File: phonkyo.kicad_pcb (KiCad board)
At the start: 2 copper layers, 65 x 30 mm, 7 parts, among them J1 GPIO, J2 AudioJack3

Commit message: finalize rev2 or v0.2
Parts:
- added C10: 2.2u, Capacitor_SMD:C_0402_1005Metric, F.Cu at (143.0, 85.5)
- added C11: 0.1u, Capacitor_SMD:C_0603_1608Metric, F.Cu at (150.0, 80.7)
- added C12: 0.1u, Capacitor_SMD:C_0402_1005Metric, F.Cu at (153.5, 82.8)
- added C13: 10uf, Capacitor_SMD:C_0603_1608Metric, F.Cu at (155.0, 83.3)
- added C2: 2.2n, Capacitor_SMD:C_0402_1005Metric, F.Cu at (143.0, 90.0)
- added C3: 2.2n, Capacitor_SMD:C_0402_1005Metric, F.Cu at (143.0, 88.0)
- added C4: 2.2u, Capacitor_SMD:C_0402_1005Metric, F.Cu at (146.0, 86.5)
- added C5: 1u, Capacitor_SMD:C_0603_1608Metric, F.Cu at (137.0, 80.0)
- added C6: 2.2n, Capacitor_SMD:C_0402_1005Metric, F.Cu at (151.5, 80.0)
- added C7: 0.1u, Capacitor_SMD:C_0603_1608Metric, F.Cu at (146.0, 81.8)
- added C8: 10uf, Capacitor_SMD:C_0603_1608Metric, F.Cu at (144.0, 81.8)
- added C9: 10uf, Capacitor_SMD:C_0603_1608Metric, F.Cu at (148.5, 80.7)
- added G***: LOGO, LOGO, F.Cu at (113.0, 91.5)
- added J4: RIJack, Connector_Audio:Jack_3.5mm_KoreanHropartsElec_PJ-320D-4A_Horizontal, F.Cu at (120.5, 91.2)
- added JP2: open, Jumper:SolderJumper-2_P1.3mm_Open_RoundedPad1.0x1.5mm, F.Cu at (162.3, 91.0)
- added R10: 22, Resistor_SMD:R_0402_1005Metric, F.Cu at (158.5, 91.0)
- added R11: 0, Resistor_SMD:R_0402_1005Metric, F.Cu at (131.5, 82.0)
- added R3: 470, Resistor_SMD:R_0402_1005Metric, F.Cu at (146.0, 88.5)
- added R4: 470, Resistor_SMD:R_0402_1005Metric, F.Cu at (146.0, 89.5)
- added R5: 10k, Resistor_SMD:R_0402_1005Metric, F.Cu at (153.5, 79.0)
- added R6: 20k, Resistor_SMD:R_0402_1005Metric, F.Cu at (152.5, 80.0)
- added R7: 22, Resistor_SMD:R_0402_1005Metric, F.Cu at (156.5, 77.5)
- added R8: 22, Resistor_SMD:R_0402_1005Metric, F.Cu at (157.5, 77.5)
- added R9: 22, Resistor_SMD:R_0402_1005Metric, F.Cu at (158.5, 90.0)
- added U2: PCM5102A, Package_SO:TSSOP-20_4.4x6.5mm_P0.65mm, F.Cu at (151.1, 88.4)
- added U3: XC6206P332MR, Package_TO_SOT_SMD:SOT-23-3, F.Cu at (140.6, 80.0)
- G***: moved to B.Cu
- J2: value AudioJack3 -> LineOutJack; footprint Connector_Audio:Jack_3.5mm_CUI_SJ-3523-SMT_Horizontal -> Connector_Audio:Jack_3.5mm_KoreanHropartsElec_PJ-320D-4A_Horizontal
- moved J2 5.31 mm to (135.0, 91.2), turned to 90 degrees
- turned G*** to 180 degrees
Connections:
- J2 pad S: GND -> GNDA
- J2 pad T: /GPIO25 -> Net-(C3-Pad2)
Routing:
- net /GPIO18/PCM.CLK: track 0.00 -> 56.5 mm, vias 0 -> 1
- net +5V: track 2.54 -> 50.1 mm, vias 0 -> 1
- net GND: track 14.2 -> 53.5 mm, vias 1 -> 9
- net +3V3: track 21.3 -> 56.8 mm, vias 0 -> 1
- net +3.3VA: track 0.00 -> 19.4 mm, vias 0 -> 2
- net Net-(C3-Pad2): track 0.00 -> 17.0 mm
- net Net-(U2-DIN): track 0.00 -> 16.8 mm
- net Net-(U2-LRCK): track 0.00 -> 16.1 mm
- net Net-(U2-XSMT): track 0.00 -> 15.4 mm
- net Net-(C2-Pad1): track 0.00 -> 15.0 mm
- net /GPIO25: track 14.2 -> 23.7 mm
- net Net-(U2-LDOO): track 0.00 -> 9.28 mm
- net Net-(U2-VNEG): track 0.00 -> 6.12 mm
- net /GPIO19/PCM.FS: track 0.00 -> 5.87 mm
- net /GPIO21/PCM.DOUT: track 0.00 -> 5.35 mm
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- added copper zone on F.Cu, net GNDA
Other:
- board text added: "Audio"
- board text added: "DAC"
- board text added: "Phonkyo v0.2"
- board text added: "Remote"
- board text added: "SCK"
- board text added: "Specs PCM5102A DAC 192kHz 24-bit RI, Line Out 2x 3.5mm Jacks"
- board text removed: "Phonkyo v0.1 Oct. 2024 Be lazier!"

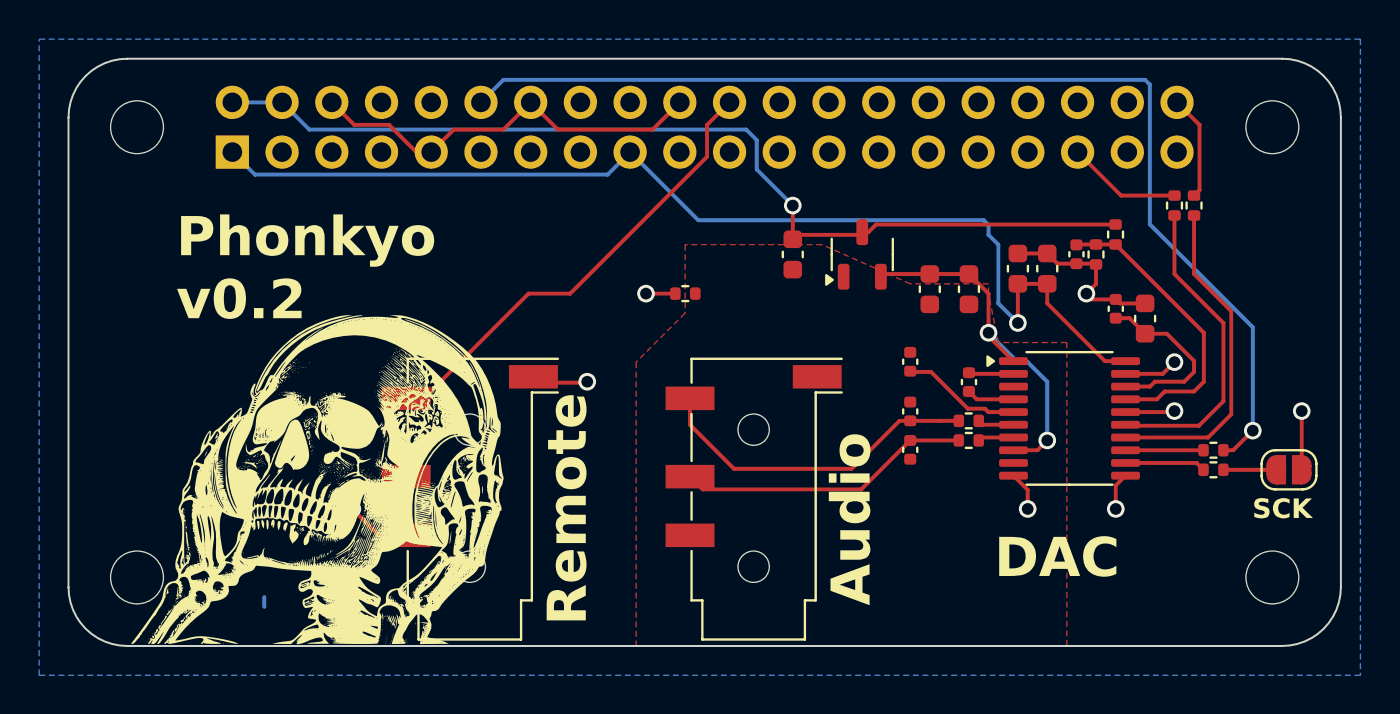
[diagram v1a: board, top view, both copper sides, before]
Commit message: finish BOM for v0.2 and submit to production
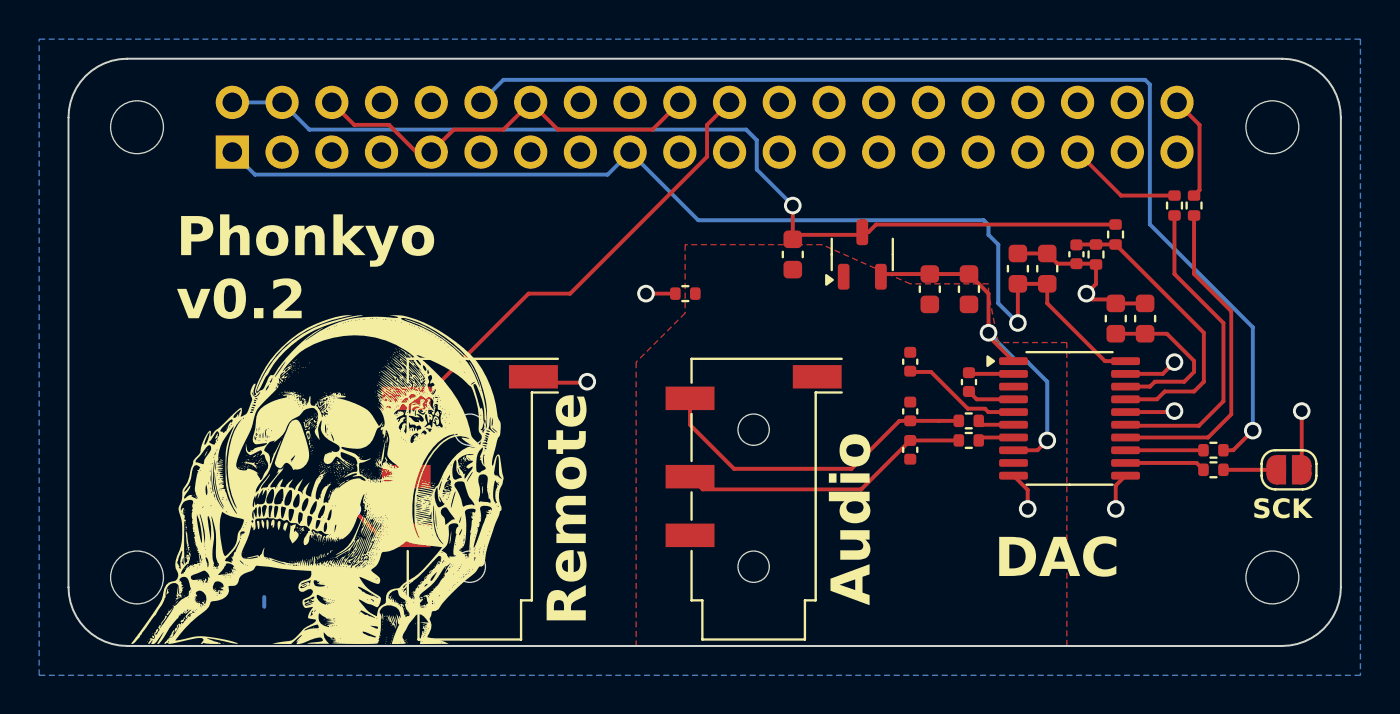
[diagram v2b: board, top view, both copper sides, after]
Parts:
- C12: footprint Capacitor_SMD:C_0402_1005Metric -> Capacitor_SMD:C_0603_1608Metric
- moved C12 0.50 mm to (153.5, 83.3)
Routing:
- net GND: track 53.5 -> 52.4 mm
- net /GPIO25: track 23.7 -> 22.8 mm
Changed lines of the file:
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@@
 			(drillshape 0)
 			(scaleselection 1)
-			(outputdirectory "production/")
+			(outputdirectory "production/v0.2")
 		)
 	)
@@
 		(tags "resistor")
 		(property "Reference" "R3"
-			(at 0 -1.17 360)
+			(at 0 -1.17 0)
 			(layer "F.SilkS")
 			(hide yes)
@@
 		)
 		(property "Value" "470"
-			(at 0 1.17 360)
+			(at 0 1.17 0)
 			(layer "F.Fab")
 			(hide yes)
@@
 		)
 		(fp_text user "${REFERENCE}"
-			(at 0 0 360)
+			(at 0 0 0)
 			(layer "F.Fab")
 			(effects
@@
 		)
 	)
-	(footprint "Capacitor_SMD:C_0402_1005Metric"
+	(footprint "Capacitor_SMD:C_0603_1608Metric"
 		(layer "F.Cu")
-		(at 153.5 82.775 90)
-		(descr "Capacitor SMD 0402 (1005 Metric), square (rectangular) end terminal, IPC_7351 nominal, (Body size source: IPC-SM-782 page 76, https://www.pcb-3d.com/wordpress/wp-content/uploads/ipc-sm-782a_amendment_1_and_2.pdf), generated with kicad-footprint-generator")
+		(at 153.5 83.275 90)
+		(descr "Capacitor SMD 0603 (1608 Metric), square (rectangular) end terminal, IPC_7351 nominal, (Body size source: IPC-SM-782 page 76, https://www.pcb-3d.com/wordpress/wp-content/uploads/ipc-sm-782a_amendment_1_and_2.pdf), generated with kicad-footprint-generator")
 		(tags "capacitor")
 		(property "Reference" "C12"
-			(at 0 -1.16 90)
+			(at 0 -1.43 90)
 			(layer "F.SilkS")
 			(hide yes)
@@
 		)
 		(property "Value" "0.1u"
-			(at 0 1.16 90)
+			(at 0 1.43 90)
 			(layer "F.Fab")
 			(hide yes)
@@
 			)
 		)
-		(property "Footprint" "Capacitor_SMD:C_0402_1005Metric"
+		(property "Footprint" "Capacitor_SMD:C_0603_1608Metric"
 			(at 0 0 90)
 			(unlocked yes)
@@
 		(attr smd)
 		(fp_line
-			(start -0.107836 -0.36)
-			(end 0.107836 -0.36)
+			(start -0.14058 -0.51)
+			(end 0.14058 -0.51)
 			(stroke
 				(width 0.12)
@@
 		)
 		(fp_line
-			(start -0.107836 0.36)
-			(end 0.107836 0.36)
+			(start -0.14058 0.51)
+			(end 0.14058 0.51)
 			(stroke
 				(width 0.12)
@@
 		)
 		(fp_line
-			(start 0.91 -0.46)
-			(end 0.91 0.46)
+			(start 1.48 -0.73)
+			(end 1.48 0.73)
 			(stroke
 				(width 0.05)
@@
 		)
 		(fp_line
-			(start -0.91 -0.46)
-			(end 0.91 -0.46)
+			(start -1.48 -0.73)
+			(end 1.48 -0.73)
 			(stroke
 				(width 0.05)
@@
 		)
 		(fp_line
-			(start 0.91 0.46)
-			(end -0.91 0.46)
+			(start 1.48 0.73)
+			(end -1.48 0.73)
 			(stroke
 				(width 0.05)
@@
 		)
 		(fp_line
-			(start -0.91 0.46)
-			(end -0.91 -0.46)
+			(start -1.48 0.73)
+			(end -1.48 -0.73)
 			(stroke
 				(width 0.05)
@@
 		)
 		(fp_line
-			(start 0.5 -0.25)
-			(end 0.5 0.25)
+			(start 0.8 -0.4)
+			(end 0.8 0.4)
 			(stroke
 				(width 0.1)
@@
 		)
 		(fp_line
-			(start -0.5 -0.25)
-			(end 0.5 -0.25)
+			(start -0.8 -0.4)
+			(end 0.8 -0.4)
 			(stroke
 				(width 0.1)
@@
 		)
 		(fp_line
-			(start 0.5 0.25)
-			(end -0.5 0.25)
+			(start 0.8 0.4)
+			(end -0.8 0.4)
 			(stroke
 				(width 0.1)
@@
 		)
 		(fp_line
-			(start -0.5 0.25)
-			(end -0.5 -0.25)
+			(start -0.8 0.4)
+			(end -0.8 -0.4)
 			(stroke
 				(width 0.1)
@@
 			(effects
 				(font
-					(size 0.25 0.25)
-					(thickness 0.04)
+					(size 0.4 0.4)
+					(thickness 0.06)
 				)
 			)
 		)
 		(pad "1" smd roundrect
-			(at -0.48 0 90)
-			(size 0.56 0.62)
+			(at -0.775 0 90)
+			(size 0.9 0.95)
 			(layers "F.Cu" "F.Paste" "F.Mask")
 			(roundrect_rratio 0.25)
@@
 		)
 		(pad "2" smd roundrect
-			(at 0.48 0 90)
-			(size 0.56 0.62)
+			(at 0.775 0 90)
+			(size 0.9 0.95)
 			(layers "F.Cu" "F.Paste" "F.Mask")
 			(roundrect_rratio 0.25)
@@
 			(pintype "passive")
 		)
-		(model "${KICAD8_3DMODEL_DIR}/Capacitor_SMD.3dshapes/C_0402_1005Metric.wrl"
+		(model "${KICAD8_3DMODEL_DIR}/Capacitor_SMD.3dshapes/C_0603_1608Metric.wrl"
 			(offset
 				(xyz 0 0 0)
@@
 		(tags "resistor")
 		(property "Reference" "R9"
-			(at 0 -1.17 360)
+			(at 0 -1.17 0)
 			(layer "F.SilkS")
 			(hide yes)
@@
 		)
 		(property "Value" "22"
-			(at 0 1.17 360)
+			(at 0 1.17 0)
 			(layer "F.Fab")
 			(hide yes)
@@
 		)
 		(fp_text user "${REFERENCE}"
-			(at 0 0 360)
+			(at 0 0 0)
 			(layer "F.Fab")
 			(effects
@@
 		(tags "resistor")
 		(property "Reference" "R11"
-			(at 0 -1.17 360)
+			(at 0 -1.17 0)
 			(layer "F.SilkS")
 			(hide yes)
@@
 		)
 		(property "Value" "0"
-			(at 0 1.17 360)
+			(at 0 1.17 0)
 			(layer "F.Fab")
 			(hide yes)
@@
 		)
 		(fp_text user "${REFERENCE}"
-			(at 0 0 360)
+			(at 0 0 0)
 			(layer "F.Fab")
 			(effects
@@
 		(tags "resistor")
 		(property "Reference" "R10"
-			(at 0 -1.17 360)
+			(at 0 -1.17 0)
 			(layer "F.SilkS")
 			(hide yes)
@@
 		)
 		(property "Value" "22"
-			(at 0 1.17 360)
+			(at 0 1.17 0)
 			(layer "F.Fab")
 			(hide yes)
@@
 		)
 		(fp_text user "${REFERENCE}"
-			(at 0 0 360)
+			(at 0 0 0)
 			(layer "F.Fab")
 			(effects
@@
 	)
 	(segment
-		(start 117.25 94.65)
-		(end 116.15 94.65)
-		(width 0.2)
-		(layer "F.Cu")
-		(net 1)
-	)
-	(segment
 		(start 118.53 74.77)
 		(end 119.68 73.62)
@@
 	)
 	(segment
-		(start 152.45 80.47)
-		(end 152.49 80.51)
-		(width 0.2)
-		(layer "F.Cu")
-		(net 1)
-	)
-	(segment
 		(start 153.705 82.5)
 		(end 153.5 82.295)
@@
 	)
 	(segment
-		(start 118.15 87.35)
-		(end 117.25 87.35)
-		(width 0.2)
-		(layer "F.Cu")
-		(net 16)
-	)
-	(segment
 		(start 132.62 75.006346)
 		(end 125.626346 82)
@@
 	)
 	(segment
-		(start 140.4125 79)
-		(end 140.55 78.8625)
-		(width 0.2)
-		(layer "F.Cu")
-		(net 30)
-	)
-	(segment
 		(start 140.55 78.8625)
 		(end 140.8625 78.8625)
@@
 	)
 	(segment
-		(start 128.95 75.03)
-		(end 128.69 74.77)
-		(width 0.2)
-		(layer "F.Cu")
-		(net 31)
-	)
-	(segment
 		(start 150 81.5)
 		(end 150 82.5)
@@
 	)
 	(segment
-		(start 141.6375 81)
-		(end 141.5 81.1375)
-		(width 0.2)
-		(layer "F.Cu")
-		(net 36)
-	)
-	(segment
 		(start 147 84.175)
 		(end 148.275 85.45)
@@
 	)
 	(segment
-		(start 146.06 86.1)
-		(end 146 86.04)
-		(width 0.2)
-		(layer "F.Cu")
-		(net 37)
-	)
-	(segment
 		(start 157.5 78.01)
 		(end 157.5 81)
@@
 	)
 	(segment
-		(start 146.65 89.35)
-		(end 146.5 89.5)
-		(width 0.2)
-		(layer "F.Cu")
-		(net 39)
-	)
-	(segment
 		(start 154 90)
 		(end 157.98 90)
@@
 	)
 	(segment
-		(start 154 88.7)
-		(end 154.05 88.75)
-		(width 0.2)
-		(layer "F.Cu")
-		(net 41)
-	)
-	(segment
 		(start 159 83.5)
 		(end 156.5 81)
@@
 	)
 	(segment
-		(start 157.98 91)
-		(end 157.83 91.15)
-		(width 0.2)
-		(layer "F.Cu")
-		(net 43)
-	)
-	(segment
 		(start 157.63 90.65)
 		(end 157.98 91)
@@
 	)
 	(segment
-		(start 151.51 79.49)
-		(end 151.49 79.51)
-		(width 0.2)
-		(layer "F.Cu")
-		(net 44)
-	)
-	(segment
 		(start 155.6 87.4)
 		(end 154 87.4)
@@
 	)
 	(segment
-		(start 151.39 79.41)
-		(end 151.49 79.51)
-		(width 0.2)
-		(layer "F.Cu")
-		(net 44)
-	)
-	(segment
 		(start 158 86.5)
 		(end 157.5 87)
@@
 	)
 	(segment
-		(start 153.5 83.255)
-		(end 154.205 83.255)
-		(width 0.2)
-		(layer "F.Cu")
-		(net 45)
-	)
-	(segment
 		(start 157 86.5)
 		(end 155.5 86.5)
@@
 	)
 	(segment
-		(start 154.205 83.255)
-		(end 155 84.05)
+		(start 155 84.05)
+		(end 153.5 84.05)
 		(width 0.2)
 		(layer "F.Cu")

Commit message: add: revision 0.3
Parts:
- removed JP2: open, Jumper:SolderJumper-2_P1.3mm_Open_RoundedPad1.0x1.5mm
- removed R10: 22, Resistor_SMD:R_0402_1005Metric
- moved R9 2.00 mm to (156.5, 90.0)
- moved C5 0.22 mm to (137.0, 79.8)
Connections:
- U2 pad 12: Net-(U2-SCK) -> GND
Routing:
- net GND: track 52.4 -> 31.9 mm
- net +5V: track 49.9 -> 54.8 mm, vias 1 -> 0
- net Net-(U2-SCK): track 4.12 -> 0.00 mm
- net +3V3: track 56.5 -> 53.2 mm, vias 1 -> 2
- net Net-(JP2-B): track 2.70 -> 0.00 mm
- net Net-(U2-BCK): track 3.98 -> 1.98 mm
- net /GPIO25: track 22.8 -> 23.8 mm, vias 0 -> 1
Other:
- board text added: "Phonkyo v0.3"
- board text removed: "Phonkyo v0.2"
- board text removed: "SCK"
